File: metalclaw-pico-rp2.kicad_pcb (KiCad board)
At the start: 4 copper layers, 21 x 51 mm, 123 parts, among them J1 USB4105-GF-A, J2 FTSH-105-01-L-DV-K, SW1 PTS810SJM250SMTR LFS, SW2 PTS810SJM250SMTR LFS, U1 XC6220B331MR-G, U2 RP2354B, U3 APS6404L-3SQR-SN, Y1 ABM8-272-T3

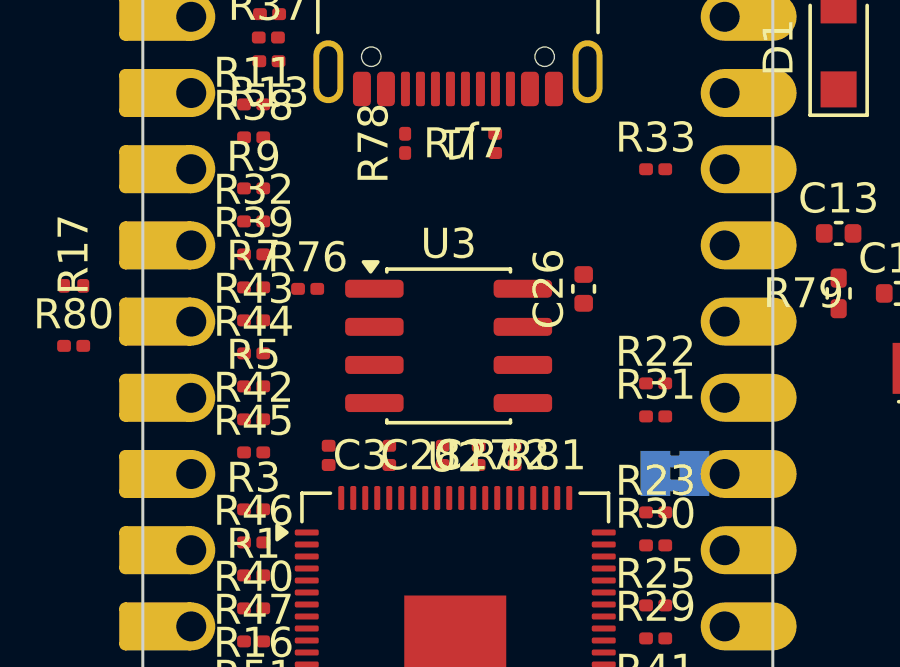
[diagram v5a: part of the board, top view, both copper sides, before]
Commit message: Set DRC and netclasses
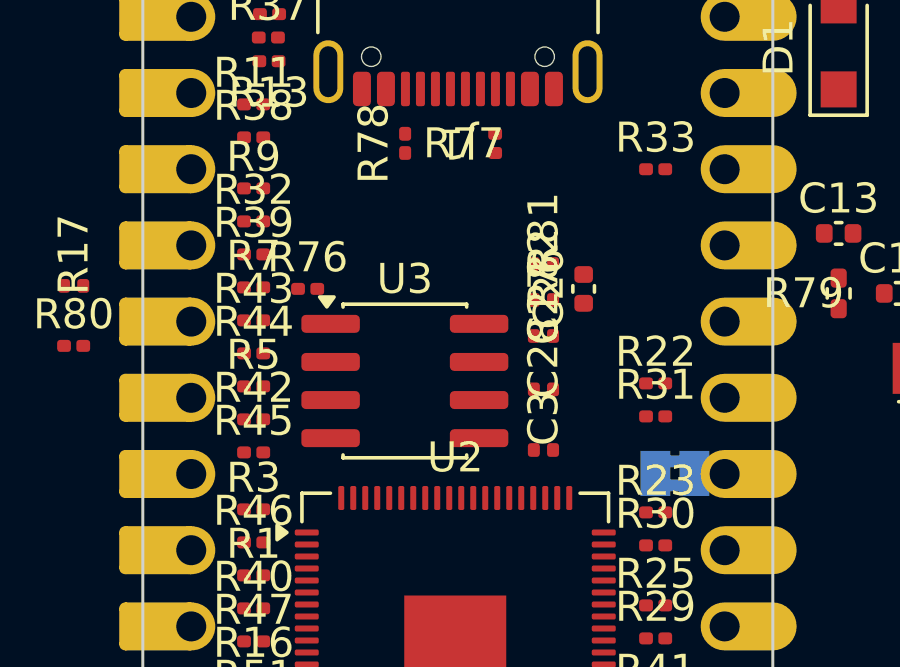
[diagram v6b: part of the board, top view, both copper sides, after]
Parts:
- moved C3 7.16 mm to (166.7, 91.7), turned to 0 degrees
- moved R81 6.45 mm to (166.7, 85.5), turned to 0 degrees
- moved R82 5.61 mm to (166.7, 86.7), turned to 0 degrees
- moved C28 5.59 mm to (166.7, 89.7), turned to 0 degrees
- moved C27 5.21 mm to (166.7, 87.9), turned to 0 degrees
- moved U3 1.87 mm to (162.0, 89.4)
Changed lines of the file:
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@@
 	(footprint "Capacitor_SMD:C_0201_0603Metric"
 		(layer "F.Cu")
-		(at 159.5 91.9 -90)
+		(at 166.66 91.72)
 		(descr "Capacitor SMD 0201 (0603 Metric), square (rectangular) end terminal, IPC-7351 nominal, (Body size source: https://www.vishay.com/docs/20052/crcw0201e3.pdf), generated with kicad-footprint-generator")
 		(tags "capacitor")
 		(property "Reference" "C3"
-			(at 0 -1.05 0)
+			(at 0 -1.05 90)
 			(layer "F.SilkS")
 			(effects
@@
 		)
 		(property "Value" "100n"
-			(at 0 1.05 0)
+			(at 0 1.05 90)
 			(layer "F.Fab")
 			(effects
@@
 		)
 		(property "Datasheet" "https://www.mouser.com/ProductDetail/KYOCERA-AVX/KGM03BR71A104KH"
-			(at 0 0 0)
+			(at 0 0 90)
 			(layer "F.Fab")
 			(hide yes)
@@
 		)
 		(property "Description" "100 nF +/-10% 10 V X7R 0201 carrier MCU decoupling capacitor, KYOCERA AVX KGM03BR71A104KH"
-			(at 0 0 0)
+			(at 0 0 90)
 			(layer "F.Fab")
 			(hide yes)
@@
 		)
 		(property "Mouser" "581-KGM03BR71A104KH"
-			(at 0 0 0)
+			(at 0 0 90)
 			(unlocked yes)
 			(layer "F.Fab")
@@
 		)
 		(property "KLC_S4.2_DVDD" ""
-			(at 0 0 0)
+			(at 0 0 90)
 			(unlocked yes)
 			(layer "F.Fab")
@@
 		)
 		(property "KLC_S4.2_VREG_LX" ""
-			(at 0 0 0)
+			(at 0 0 90)
 			(unlocked yes)
 			(layer "F.Fab")
@@
 		)
 		(fp_text user "${REFERENCE}"
-			(at 0 -0.68 0)
+			(at 0 -0.68 90)
 			(layer "F.Fab")
 			(effects
@@
 		)
 		(pad "" smd roundrect
-			(at -0.345 0)
+			(at -0.345 0 90)
 			(size 0.318 0.36)
 			(layers "F.Paste")
@@
 		)
 		(pad "" smd roundrect
-			(at 0.345 0)
+			(at 0.345 0 90)
 			(size 0.318 0.36)
 			(layers "F.Paste")
@@
 		)
 		(pad "1" smd roundrect
-			(at -0.32 0)
+			(at -0.32 0 90)
 			(size 0.46 0.4)
 			(layers "F.Cu" "F.Mask")
@@
 		)
 		(pad "2" smd roundrect
-			(at 0.32 0)
+			(at 0.32 0 90)
 			(size 0.46 0.4)
 			(layers "F.Cu" "F.Mask")
@@
 	(footprint "Resistor_SMD:R_0201_0603Metric"
 		(layer "F.Cu")
-		(at 165.7 91.9 -90)
+		(at 166.66 85.52)
 		(descr "Resistor SMD 0201 (0603 Metric), square (rectangular) end terminal, IPC-7351 nominal, (Body size source: https://www.vishay.com/docs/20052/crcw0201e3.pdf), generated with kicad-footprint-generator")
 		(tags "resistor")
 		(property "Reference" "R81"
-			(at 0 -1.05 0)
+			(at 0 -1.05 90)
 			(layer "F.SilkS")
 			(effects
@@
 		)
 		(property "Value" "27"
-			(at 0 1.05 0)
+			(at 0 1.05 90)
 			(layer "F.Fab")
 			(effects
@@
 		)
 		(property "Datasheet" "https://www.mouser.com/ProductDetail/YAGEO/RC0201FR-0727RL"
-			(at 0 0 0)
+			(at 0 0 90)
 			(layer "F.Fab")
 			(hide yes)
@@
 		)
 		(property "Description" "27 ohm +/-1% 1/20 W 0201 USB data series resistor, Yageo RC0201FR-0727RL"
-			(at 0 0 0)
+			(at 0 0 90)
 			(layer "F.Fab")
 			(hide yes)
@@
 		)
 		(property "Mouser" "603-RC0201FR-0727RL"
-			(at 0 0 0)
+			(at 0 0 90)
 			(unlocked yes)
 			(layer "F.Fab")
@@
 		)
 		(property "KLC_S4.2_DVDD" ""
-			(at 0 0 0)
+			(at 0 0 90)
 			(unlocked yes)
 			(layer "F.Fab")
@@
 		)
 		(property "KLC_S4.2_VREG_LX" ""
-			(at 0 0 0)
+			(at 0 0 90)
 			(unlocked yes)
 			(layer "F.Fab")
@@
 		)
 		(fp_text user "${REFERENCE}"
-			(at 0 -0.68 0)
+			(at 0 -0.68 90)
 			(layer "F.Fab")
 			(effects
@@
 		)
 		(pad "" smd roundrect
-			(at -0.345 0)
+			(at -0.345 0 90)
 			(size 0.318 0.36)
 			(layers "F.Paste")
@@
 		)
 		(pad "" smd roundrect
-			(at 0.345 0)
+			(at 0.345 0 90)
 			(size 0.318 0.36)
 			(layers "F.Paste")
@@
 		)
 		(pad "1" smd roundrect
-			(at -0.32 0)
+			(at -0.32 0 90)
 			(size 0.46 0.4)
 			(layers "F.Cu" "F.Mask")
@@
 		)
 		(pad "2" smd roundrect
-			(at 0.32 0)
+			(at 0.32 0 90)
 			(size 0.46 0.4)
 			(layers "F.Cu" "F.Mask")
@@
 	(footprint "Capacitor_SMD:C_0201_0603Metric"
 		(layer "F.Cu")
-		(at 161.52 91.9 -90)
+		(at 166.66 89.7)
 		(descr "Capacitor SMD 0201 (0603 Metric), square (rectangular) end terminal, IPC-7351 nominal, (Body size source: https://www.vishay.com/docs/20052/crcw0201e3.pdf), generated with kicad-footprint-generator")
 		(tags "capacitor")
 		(property "Reference" "C28"
-			(at 0 -1.05 0)
+			(at 0 -1.05 90)
 			(layer "F.SilkS")
 			(effects
@@
 		)
 		(property "Value" "100n"
-			(at 0 1.05 0)
+			(at 0 1.05 90)
 			(layer "F.Fab")
 			(effects
@@
 		)
 		(property "Datasheet" "https://www.mouser.com/ProductDetail/KYOCERA-AVX/KGM03BR71A104KH"
-			(at 0 0 0)
+			(at 0 0 90)
 			(layer "F.Fab")
 			(hide yes)
@@
 		)
 		(property "Description" "100 nF +/-10% 10 V X7R 0201 carrier MCU decoupling capacitor, KYOCERA AVX KGM03BR71A104KH"
-			(at 0 0 0)
+			(at 0 0 90)
 			(layer "F.Fab")
 			(hide yes)
@@
 		)
 		(property "Mouser" "581-KGM03BR71A104KH"
-			(at 0 0 0)
+			(at 0 0 90)
 			(unlocked yes)
 			(layer "F.Fab")
@@
 		)
 		(property "KLC_S4.2_DVDD" ""
-			(at 0 0 0)
+			(at 0 0 90)
 			(unlocked yes)
 			(layer "F.Fab")
@@
 		)
 		(property "KLC_S4.2_VREG_LX" ""
-			(at 0 0 0)
+			(at 0 0 90)
 			(unlocked yes)
 			(layer "F.Fab")
@@
 		)
 		(fp_text user "${REFERENCE}"
-			(at 0 -0.68 0)
+			(at 0 -0.68 90)
 			(layer "F.Fab")
 			(effects
@@
 		)
 		(pad "" smd roundrect
-			(at -0.345 0)
+			(at -0.345 0 90)
 			(size 0.318 0.36)
 			(layers "F.Paste")
@@
 		)
 		(pad "" smd roundrect
-			(at 0.345 0)
+			(at 0.345 0 90)
 			(size 0.318 0.36)
 			(layers "F.Paste")
@@
 		)
 		(pad "1" smd roundrect
-			(at -0.32 0)
+			(at -0.32 0 90)
 			(size 0.46 0.4)
 			(layers "F.Cu" "F.Mask")
@@
 		)
 		(pad "2" smd roundrect
-			(at 0.32 0)
+			(at 0.32 0 90)
 			(size 0.46 0.4)
 			(layers "F.Cu" "F.Mask")
@@
 	(footprint "Resistor_SMD:R_0201_0603Metric"
 		(layer "F.Cu")
-		(at 164.5 91.9 -90)
+		(at 166.66 86.72)
 		(descr "Resistor SMD 0201 (0603 Metric), square (rectangular) end terminal, IPC-7351 nominal, (Body size source: https://www.vishay.com/docs/20052/crcw0201e3.pdf), generated with kicad-footprint-generator")
 		(tags "resistor")
 		(property "Reference" "R82"
-			(at 0 -1.05 0)
+			(at 0 -1.05 90)
 			(layer "F.SilkS")
 			(effects
@@
 		)
 		(property "Value" "27"
-			(at 0 1.05 0)
+			(at 0 1.05 90)
 			(layer "F.Fab")
 			(effects
@@
 		)
 		(property "Datasheet" "https://www.mouser.com/ProductDetail/YAGEO/RC0201FR-0727RL"
-			(at 0 0 0)
+			(at 0 0 90)
 			(layer "F.Fab")
 			(hide yes)
@@
 		)
 		(property "Description" "27 ohm +/-1% 1/20 W 0201 USB data series resistor, Yageo RC0201FR-0727RL"
-			(at 0 0 0)
+			(at 0 0 90)
 			(layer "F.Fab")
 			(hide yes)
@@
 		)
 		(property "Mouser" "603-RC0201FR-0727RL"
-			(at 0 0 0)
+			(at 0 0 90)
 			(unlocked yes)
 			(layer "F.Fab")
@@
 		)
 		(property "KLC_S4.2_DVDD" ""
-			(at 0 0 0)
+			(at 0 0 90)
 			(unlocked yes)
 			(layer "F.Fab")
@@
 		)
 		(property "KLC_S4.2_VREG_LX" ""
-			(at 0 0 0)
+			(at 0 0 90)
 			(unlocked yes)
 			(layer "F.Fab")
@@
 		)
 		(fp_text user "${REFERENCE}"
-			(at 0 -0.68 0)
+			(at 0 -0.68 90)
 			(layer "F.Fab")
 			(effects
@@
 		)
 		(pad "" smd roundrect
-			(at -0.345 0)
+			(at -0.345 0 90)
 			(size 0.318 0.36)
 			(layers "F.Paste")
@@
 		)
 		(pad "" smd roundrect
-			(at 0.345 0)
+			(at 0.345 0 90)
 			(size 0.318 0.36)
 			(layers "F.Paste")
@@
 		)
 		(pad "1" smd roundrect
-			(at -0.32 0)
+			(at -0.32 0 90)
 			(size 0.46 0.4)
 			(layers "F.Cu" "F.Mask")
@@
 		)
 		(pad "2" smd roundrect
-			(at 0.32 0)
+			(at 0.32 0 90)
 			(size 0.46 0.4)
 			(layers "F.Cu" "F.Mask")
@@
 	(footprint "Package_SO:SOIC-8_3.9x4.9mm_P1.27mm"
 		(layer "F.Cu")
-		(at 163.5 88.25)
+		(at 162.04 89.42)
 		(descr "SOIC, 8 Pin (JEDEC MS-012AA, https://www.analog.com/media/en/package-pcb-resources/package/pkg_pdf/soic_narrow-r/r_8.pdf), generated with kicad-footprint-generator ipc_gullwing_generator.py")
 		(tags "SOIC SO")
@@
 	(footprint "Capacitor_SMD:C_0201_0603Metric"
 		(layer "F.Cu")
-		(at 163.3 91.9 -90)
+		(at 166.66 87.92)
 		(descr "Capacitor SMD 0201 (0603 Metric), square (rectangular) end terminal, IPC-7351 nominal, (Body size source: https://www.vishay.com/docs/20052/crcw0201e3.pdf), generated with kicad-footprint-generator")
 		(tags "capacitor")
 		(property "Reference" "C27"
-			(at 0 -1.05 0)
+			(at 0 -1.05 90)
 			(layer "F.SilkS")
 			(effects
@@
 		)
 		(property "Value" "100n"
-			(at 0 1.05 0)
+			(at 0 1.05 90)
 			(layer "F.Fab")
 			(effects
@@
 		)
 		(property "Datasheet" "https://www.mouser.com/ProductDetail/KYOCERA-AVX/KGM03BR71A104KH"
-			(at 0 0 0)
+			(at 0 0 90)
 			(layer "F.Fab")
 			(hide yes)
@@
 		)
 		(property "Description" "100 nF +/-10% 10 V X7R 0201 carrier MCU decoupling capacitor, KYOCERA AVX KGM03BR71A104KH"
-			(at 0 0 0)
+			(at 0 0 90)
 			(layer "F.Fab")
 			(hide yes)
@@
 		)
 		(property "Mouser" "581-KGM03BR71A104KH"
-			(at 0 0 0)
+			(at 0 0 90)
 			(unlocked yes)
 			(layer "F.Fab")
@@
 		)
 		(property "KLC_S4.2_DVDD" ""
-			(at 0 0 0)
+			(at 0 0 90)
 			(unlocked yes)
 			(layer "F.Fab")
@@
 		)
 		(property "KLC_S4.2_VREG_LX" ""
-			(at 0 0 0)
+			(at 0 0 90)
 			(unlocked yes)
 			(layer "F.Fab")
@@
 		)
 		(fp_text user "${REFERENCE}"
-			(at 0 -0.68 0)
+			(at 0 -0.68 90)
 			(layer "F.Fab")
 			(effects
@@
 		)
 		(pad "" smd roundrect
-			(at -0.345 0)
+			(at -0.345 0 90)
 			(size 0.318 0.36)
 			(layers "F.Paste")
@@
 		)
 		(pad "" smd roundrect
-			(at 0.345 0)
+			(at 0.345 0 90)
 			(size 0.318 0.36)
 			(layers "F.Paste")
@@
 		)
 		(pad "1" smd roundrect
-			(at -0.32 0)
+			(at -0.32 0 90)
 			(size 0.46 0.4)
 			(layers "F.Cu" "F.Mask")
@@
 		)
 		(pad "2" smd roundrect
-			(at 0.32 0)
+			(at 0.32 0 90)
 			(size 0.46 0.4)
 			(layers "F.Cu" "F.Mask")

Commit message: More initial rough placement
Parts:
- moved C21 28.5 mm to (157.4, 100.7)
- moved C22 23.6 mm to (164.9, 106.3), turned to 180 degrees
- moved C2 18.4 mm to (167.7, 88.1), turned to 180 degrees
- moved C10 18.0 mm to (170.1, 88.0)
- moved C8 17.9 mm to (170.2, 100.2)
- moved C14 16.5 mm to (166.7, 94.1), turned to 180 degrees
- moved C4 15.8 mm to (170.2, 89.8)
- moved U1 14.4 mm to (167.8, 85.1)
- moved C1 13.9 mm to (167.8, 82.1)
- moved L1 12.7 mm to (167.1, 91.5)
- moved SW2 11.3 mm to (159.9, 109.6)
- moved C20 10.9 mm to (170.1, 94.9), turned to 180 degrees
- moved C15 8.99 mm to (157.5, 96.1)
- moved C7 8.60 mm to (177.6, 96.2), turned to -90 degrees
- moved R30 6.97 mm to (177.4, 94.8)
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
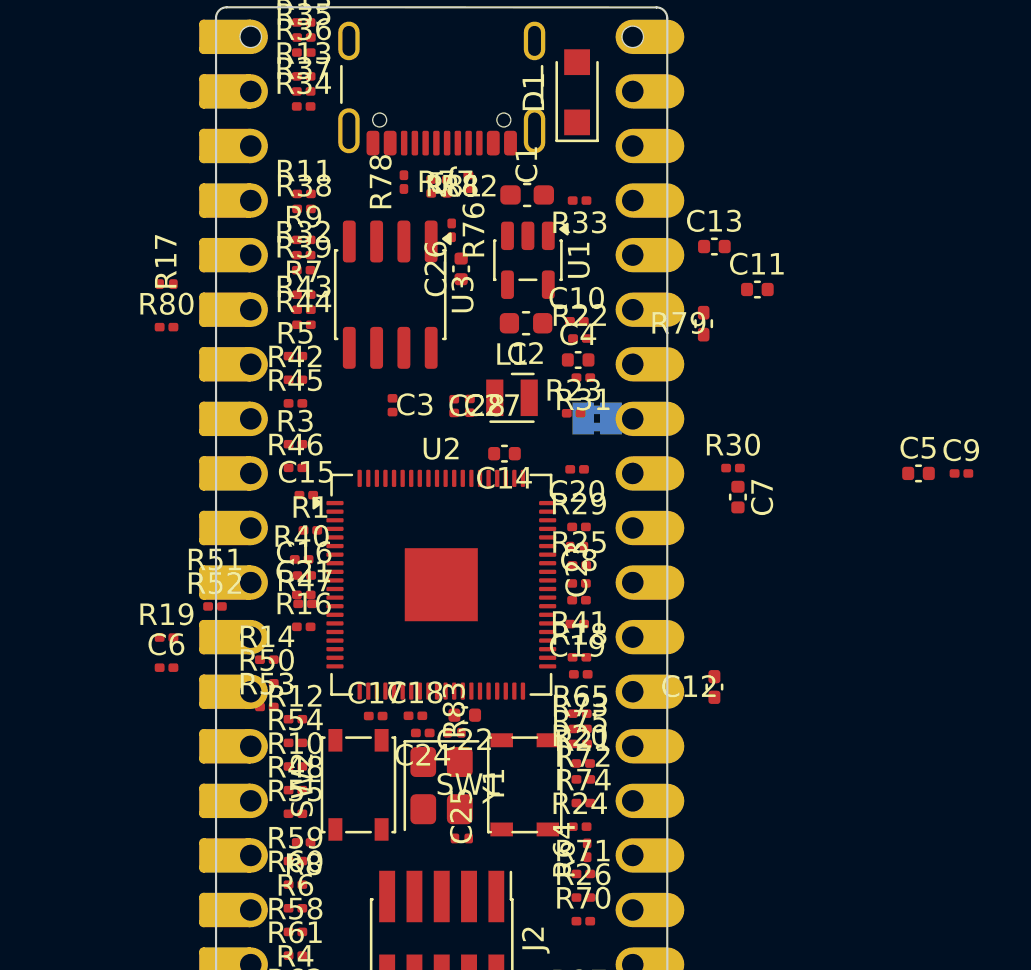
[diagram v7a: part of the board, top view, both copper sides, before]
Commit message: Fit all components inside board
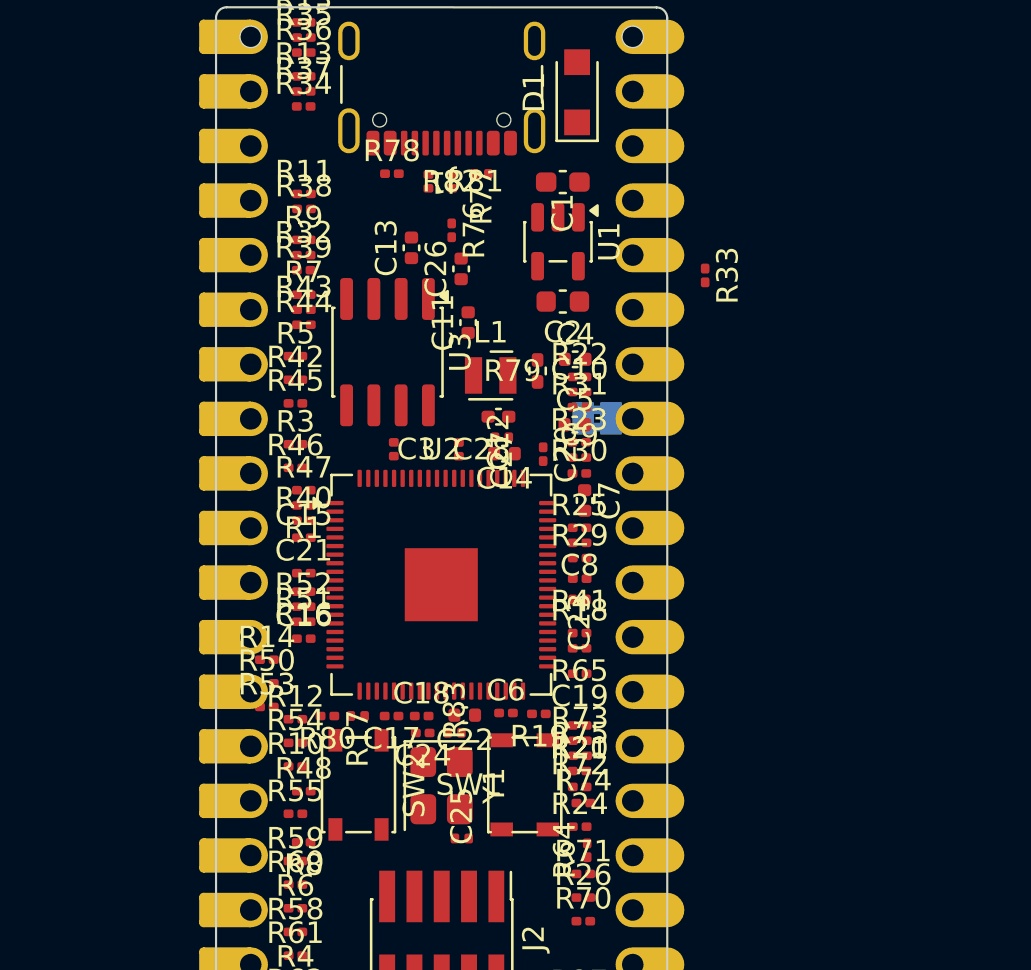
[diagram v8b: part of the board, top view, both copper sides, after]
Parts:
- moved R17 22.0 mm to (159.9, 106.3), turned to 180 degrees
- moved R80 19.6 mm to (158.5, 106.3), turned to 180 degrees
- moved C9 17.8 mm to (170.2, 94.3)
- moved R19 17.7 mm to (168.3, 106.2), turned to 180 degrees
- moved C5 16.2 mm to (170.0, 92.8)
- moved C12 16.1 mm to (166.4, 92.4), turned to 180 degrees
- moved C6 15.9 mm to (166.8, 106.2)
- moved C13 14.1 mm to (162.4, 84.6), turned to 90 degrees
- moved C11 13.5 mm to (165.0, 88.0), turned to 90 degrees
- moved R79 8.04 mm to (168.3, 90.3)
- moved R30 7.15 mm to (170.2, 95.1)
- moved C7 7.14 mm to (170.5, 96.3)
- moved R33 6.81 mm to (176.1, 85.8), turned to -90 degrees
- moved R47 5.29 mm to (157.4, 95.8)
- moved R51 4.51 mm to (157.4, 102.0)
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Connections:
- SW1 pad 2: Net-(R80-Pad2) -> /RESET
- SW2 pad 2: /RESET -> Net-(R80-Pad2)
